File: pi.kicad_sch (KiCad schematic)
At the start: 1 part, among them J1 Raspberry_Pi_2_3

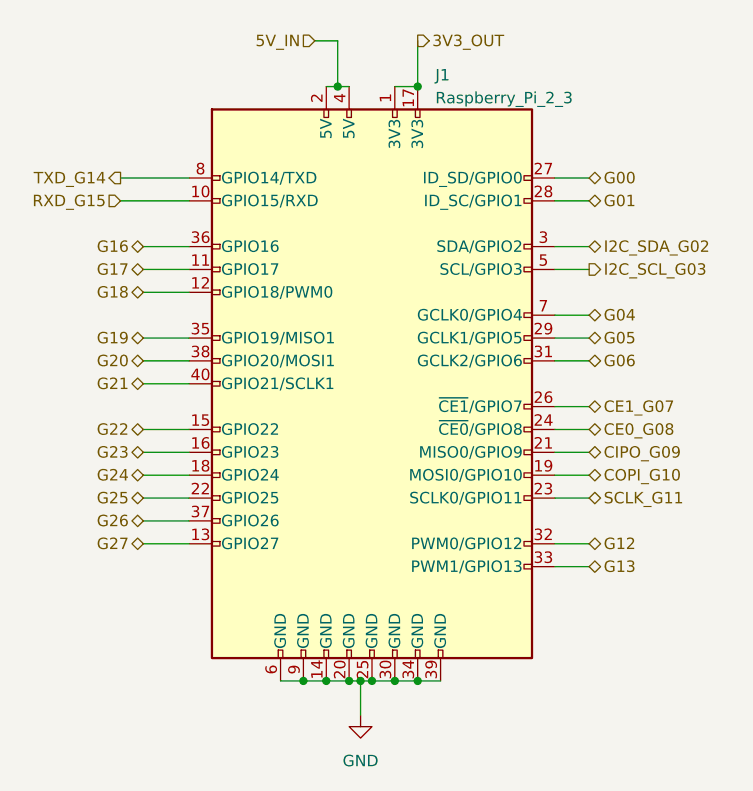
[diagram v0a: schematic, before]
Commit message: Build pogoplayground v1.0 - Fix continuity tester reference voltage - Fix SSR 5V supply
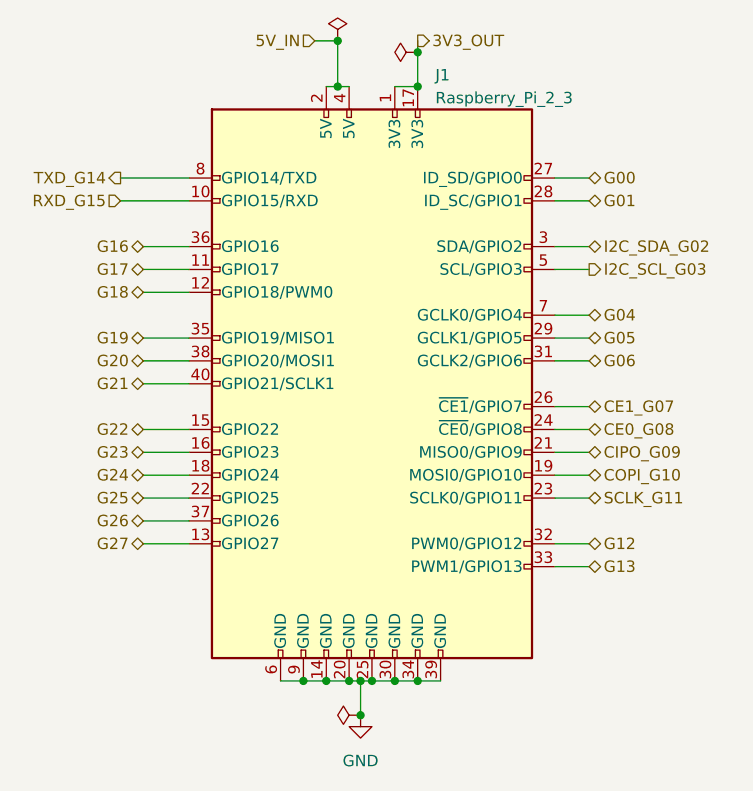
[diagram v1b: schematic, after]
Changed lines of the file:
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@@
   (junction (at 85.09 154.94) (diameter 0) (color 0 0 0 0)
   )
+  (junction (at 95.25 85.09) (diameter 0) (color 0 0 0 0)
+  )
   (junction (at 95.25 88.9) (diameter 0) (color 0 0 0 0)
   )
@@
   (junction (at 95.25 154.94) (diameter 0) (color 0 0 0 0)
   )
+  (junction (at 86.36 83.82) (diameter 0) (color 0 0 0 0)
+  )
   (junction (at 82.55 154.94) (diameter 0) (color 0 0 0 0)
   )
+  (junction (at 88.9 158.75) (diameter 0) (color 0 0 0 0)
+  )
   (wire (pts (xy 85.09 154.94) (xy 87.63 154.94))
     (stroke (width 0) (type default))
@@
     (stroke (width 0) (type default))
   )
-  (wire (pts (xy 95.25 83.82) (xy 95.25 88.9))
+  (wire (pts (xy 95.25 83.82) (xy 95.25 85.09))
     (stroke (width 0) (type default))
   )
@@
     (stroke (width 0) (type default))
   )
+  (wire (pts (xy 95.25 85.09) (xy 95.25 88.9))
+    (stroke (width 0) (type default))
+  )
   (wire (pts (xy 88.9 154.94) (xy 90.17 154.94))
     (stroke (width 0) (type default))
@@
   (hierarchical_label "I2C_SCL_G03" (shape output) (at 114.3 109.22 0) (fields_autoplaced)
     (effects (font (size 1.27 1.27)) (justify left))
+  )
+  (symbol (lib_id "power:PWR_FLAG") (at 86.36 83.82 0) (unit 1)
+    (in_bom yes) (on_board yes) (dnp no) (fields_autoplaced)
+    (property "Reference" "#FLG01" (at 86.36 81.915 0)
+      (effects (font (size 1.27 1.27)) hide)
+    )
+    (property "Value" "PWR_FLAG" (at 86.36 78.74 0)
+      (effects (font (size 1.27 1.27)) hide)
+    )
+    (property "Footprint" "" (at 86.36 83.82 0)
+      (effects (font (size 1.27 1.27)) hide)
+    )
+    (property "Datasheet" "~" (at 86.36 83.82 0)
+      (effects (font (size 1.27 1.27)) hide)
+    )
+    (pin "1")
+    (instances
+      (project "pogoplayground"
+        (path "/086fca78-0381-464b-8bbb-5a6257773e1c"
+          (reference "#FLG01") (unit 1)
+        )
+        (path "/086fca78-0381-464b-8bbb-5a6257773e1c/d93413af-9331-4b93-bb3a-470b27813c8d"
+          (reference "#FLG04") (unit 1)
+        )
+      )
+    )
   )
   (symbol (lib_id "Connector:Raspberry_Pi_2_3") (at 90.17 121.92 0) (unit 1)
@@
     )
   )
+  (symbol (lib_id "power:PWR_FLAG") (at 88.9 158.75 90) (unit 1)
+    (in_bom yes) (on_board yes) (dnp no) (fields_autoplaced)
+    (property "Reference" "#FLG01" (at 86.995 158.75 0)
+      (effects (font (size 1.27 1.27)) hide)
+    )
+    (property "Value" "PWR_FLAG" (at 83.82 158.75 0)
+      (effects (font (size 1.27 1.27)) hide)
+    )
+    (property "Footprint" "" (at 88.9 158.75 0)
+      (effects (font (size 1.27 1.27)) hide)
+    )
+    (property "Datasheet" "~" (at 88.9 158.75 0)
+      (effects (font (size 1.27 1.27)) hide)
+    )
+    (pin "1")
+    (instances
+      (project "pogoplayground"
+        (path "/086fca78-0381-464b-8bbb-5a6257773e1c"
+          (reference "#FLG01") (unit 1)
+        )
+        (path "/086fca78-0381-464b-8bbb-5a6257773e1c/d93413af-9331-4b93-bb3a-470b27813c8d"
+          (reference "#FLG06") (unit 1)
+        )
+      )
+    )
+  )
   (symbol (lib_id "power:GND") (at 88.9 158.75 0) (unit 1)
     (in_bom yes) (on_board yes) (dnp no) (fields_autoplaced)
@@
         )
       )
+    )
+  )
+  (symbol (lib_id "power:PWR_FLAG") (at 95.25 85.09 90) (unit 1)
+    (in_bom yes) (on_board yes) (dnp no) (fields_autoplaced)
+    (property "Reference" "#FLG01" (at 93.345 85.09 0)
+      (effects (font (size 1.27 1.27)) hide)
+    )
+    (property "Value" "PWR_FLAG" (at 90.17 85.09 0)
+      (effects (font (size 1.27 1.27)) hide)
+    )
+    (property "Footprint" "" (at 95.25 85.09 0)
+      (effects (font (size 1.27 1.27)) hide)
+    )
+    (property "Datasheet" "~" (at 95.25 85.09 0)
+      (effects (font (size 1.27 1.27)) hide)
+    )
+    (pin "1")
+    (instances
+      (project "pogoplayground"
+        (path "/086fca78-0381-464b-8bbb-5a6257773e1c"
+          (reference "#FLG01") (unit 1)
+        )
+        (path "/086fca78-0381-464b-8bbb-5a6257773e1c/d93413af-9331-4b93-bb3a-470b27813c8d"
+          (reference "#FLG05") (unit 1)
+        )
+      )
